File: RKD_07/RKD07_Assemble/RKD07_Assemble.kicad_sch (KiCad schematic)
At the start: 147 parts, among them J1 Conn_01x02_Socket, J2 Conn_01x24, J3 Conn_01x24, J4 Conn_01x24, SW1 SW_Push, SW10 SW_Push, SW11 SW_Push, SW12 SW_Push, SW13 SW_Push, SW14 SW_Push, SW15 SW_Push, SW16 SW_Push, SW17 SW_Push, SW18 SW_Push, SW19 SW_Push, SW2 SW_Push, SW20 SW_Push, SW21 SW_Push, SW22 SW_Push, SW23 SW_Push, SW24 SW_Push, SW25 SW_Push, SW26 SW_Push, SW27 SW_Push, SW28 SW_Push, SW29 SW_Push, SW3 SW_Push, SW30 RotaryEncoder_Switch, SW31 SW_Push, SW4 SW_Push, SW5 SW_Push, SW51 SW_Push, SW52 SW_Push, SW53 SW_Push, SW54 SW_Push, SW55 SW_Push, SW56 SW_Push, SW57 SW_Push, SW58 SW_Push, SW59 SW_Push, SW6 SW_Push, SW60 SW_Push, SW61 SW_Push, SW62 SW_Push, SW63 SW_Push, SW64 SW_Push, SW65 SW_Push, SW66 SW_Push, SW67 SW_Push, SW68 SW_Push, SW69 SW_Push, SW7 SW_Push, SW70 SW_Push, SW71 SW_Push, SW72 SW_Push, SW73 SW_Push, SW74 SW_Push, SW75 SW_Push, SW76 SW_Push, SW77 SW_Push, SW78 SW_Push, SW79 SW_Push, SW8 SW_Push, SW80 SW_Push, SW81 SW_Push, SW82 SW_Push, SW83 SW_Push, SW84 SW_Push, SW85 SW_Push, SW86 SW_Push, SW87 SW_Push, SW88 SW_Push, SW89 SW_Push, SW9 SW_Push, SW90 SW_Push, U1 Pico

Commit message: RKD07 一時保存
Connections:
- net GP18_R is gone; now on net SDA/SCK_R: J3.14 (Pin_14), J4.11 (Pin_11)
- net GP19_R is gone; now on net SCL/TX_R: J3.13 (Pin_13), J4.12 (Pin_12)
- net GND_L: now also U1.23 (GND)
- net SCL/TX_L: now also J2.12 (Pin_12), U1.25 (GPIO19); no longer J2.1 (Pin_1), U1.20 (GPIO15)
- net SCL/TX_R: no longer J3.24 (Pin_24), J4.1 (Pin_1)
- net SDA/SCK_L: now also J2.11 (Pin_11), U1.24 (GPIO18); no longer J2.2 (Pin_2), U1.19 (GPIO14)
- net SDA/SCK_R: no longer J3.23 (Pin_23), J4.2 (Pin_2)
- new net GP14_R: J3.23 (Pin_23), J4.2 (Pin_2)
- new net GP15_R: J3.24 (Pin_24), J4.1 (Pin_1)
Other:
- note added: "GND VCC 3V3 GP28 GP27 GP26 GP25 GP24 GP23 GP22 GP21 GP20 GP19 GP18 GP17 GP16 GP08 GP09 GP10 GP11 GP12 GP13 GP14 GP15"
- moved on the sheet: J2

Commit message: RD07配線
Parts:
- added J10, J9: Conn_01x04, Connector_PinSocket_2.54mm:PinSocket_1x04_P2.54mm_Horizontal, symbol Connector_Generic:Conn_01x04
- added J5, J6: Qwiic_RA, SparkFun-Connector:JST_SMD_1.0mm-4_Black, symbol SparkFun-Connector:Qwiic_Right_Angle
- added J7, J8: Conn_01x06, Connector_FFC-FPC:Hirose_FH12-6S-0.5SH_1x06-1MP_P0.50mm_Horizontal, symbol Connector_Generic:Conn_01x06
- added R1, R2: R, Resistor_THT:R_Axial_DIN0207_L6.3mm_D2.5mm_P10.16mm_Horizontal, symbol Device:R
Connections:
- net GP12_R is gone; now on net ROW1_R: J3.21 (Pin_21), J4.4 (Pin_4)
- net GP13_R is gone; now on net ROW2_R: J3.22 (Pin_22), J4.3 (Pin_3)
- net GP14_R is gone; now on net ROW3_R: J3.23 (Pin_23), J4.2 (Pin_2)
- net GP15_R is gone; now on net ROW4_R: J3.24 (Pin_24), J4.1 (Pin_1)
- net GP20_R is gone; now on net COL6_R: J3.12 (Pin_12), J4.13 (Pin_13)
- net GP21_R is gone; now on net COL7_R: J3.11 (Pin_11), J4.14 (Pin_14)
- net GP22_R is gone; now on net COL8_R: J3.10 (Pin_10), J4.15 (Pin_15)
- net GP23_R is gone; now on net COL9_R: J3.9 (Pin_9), J4.16 (Pin_16)
- net GP24_R is gone; now on net COL10_R: J3.8 (Pin_8), J4.17 (Pin_17)
- net GP25_R is gone; now on net COL11_R: J3.7 (Pin_7), J4.18 (Pin_18)
- net GP26_R is gone; now on net COL12_R: J3.6 (Pin_6), J4.19 (Pin_19)
- net GP27_R is gone; now on net COL13_R: J3.5 (Pin_5), J4.20 (Pin_20)
- net GP28_R is gone; now on net ROW0_R: J3.4 (Pin_4), J4.21 (Pin_21)
- net 3v3_L: now also J5.2 (Pin_2), J8.6 (Pin_6)
- net 3v3_R: now also J6.2 (Pin_2), J7.6 (Pin_6), J9.2 (Pin_2), J9.3 (Pin_3), R1.1, R2.1
- net COL0_L: now also J2.10 (Pin_10), U1.2 (GPIO1)
- net COL1_L: now also J2.9 (Pin_9), U1.4 (GPIO2)
- net COL2_L: now also J2.8 (Pin_8), U1.5 (GPIO3)
- net COL3_L: now also J2.7 (Pin_7), U1.6 (GPIO4)
- net COL4_L: now also J2.6 (Pin_6), U1.7 (GPIO5)
- net COL5_L: now also J2.5 (Pin_5), U1.9 (GPIO6)
- net GND_L: now also U1.28 (GND), J5.1 (Pin_1), J8.1 (Pin_1), J8.5 (Pin_5)
- net GND_R: now also J6.1 (Pin_1), J7.1 (Pin_1), J7.5 (Pin_5)
- net RE_A: now also U1.15 (GPIO11), J10.1 (Pin_1)
- net RE_B: now also U1.16 (GPIO12), J10.4 (Pin_4)
- net ROW0_L: now also J2.21 (Pin_21), U1.1 (GPIO0)
- net ROW1_L: now also J2.4 (Pin_4), U1.10 (GPIO7)
- net ROW2_L: now also J2.3 (Pin_3), U1.11 (GPIO8)
- net ROW3_L: now also J2.2 (Pin_2), U1.12 (GPIO9)
- net ROW4_L: now also J2.1 (Pin_1), U1.14 (GPIO10)
- net SCL/TX_L: now also J10.3 (Pin_3), J5.4 (Pin_4)
- net SCL/TX_R: now also J6.4 (Pin_4), J7.3 (Pin_3), J9.1 (Pin_1), R1.2
- net SDA/SCK_L: now also J10.2 (Pin_2), J5.3 (Pin_3)
- net SDA/SCK_R: now also J6.3 (Pin_3), J7.2 (Pin_2), J9.4 (Pin_4), R2.2
- net SCK_L: now reaches U1.19 (GPIO14)
- net SCK_L: now also J8.2 (Pin_2)
- net TX_L: now reaches U1.20 (GPIO15)
- net TX_L: now also J8.3 (Pin_3)
- net COL6_L: now reaches U1.21 (GPIO16)
- net COL6_L: now also J2.13 (Pin_13)
- net COL7_L: now reaches U1.22 (GPIO17)
- net COL7_L: now also J2.14 (Pin_14)
- net COL8_L: now reaches U1.26 (GPIO20)
- net COL8_L: now also J2.15 (Pin_15)
- net COL9_L: now reaches U1.27 (GPIO21)
- net COL9_L: now also J2.16 (Pin_16)
- net COL10_L: now reaches U1.29 (GPIO22)
- net COL10_L: now also J2.17 (Pin_17)
- net COL11_L: now reaches U1.31 (GPIO26_ADC0)
- net COL11_L: now also J2.18 (Pin_18)
- net COL12_L: now reaches U1.32 (GPIO27_ADC1)
- net COL12_L: now also J2.19 (Pin_19)
- net COL13_L: now reaches U1.34 (GPIO28_ADC2)
- net COL13_L: now also J2.20 (Pin_20)
- net GP08_R renamed COL2_R
- net GP09_R renamed COL3_R
- net GP10_R renamed COL4_R
- net GP11_R renamed COL5_R
- net GP16_R renamed COL1_R
- net GP17_R renamed COL0_R
- no-connect marks 8 -> 15
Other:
- note added: "CS"
- note added: "MOTION"
- note added: "Resist for i2c"

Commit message: 07 Modify
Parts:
- J10: footprint Connector_PinSocket_2.54mm:PinSocket_1x04_P2.54mm_Horizontal -> Connector_PinHeader_2.54mm:PinHeader_1x04_P2.54mm_Horizontal
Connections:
- net RE_A: now also J10.4 (Pin_4); no longer J10.1 (Pin_1)
- net RE_B: now also J10.1 (Pin_1); no longer J10.4 (Pin_4)
- net SCL/TX_L: now also J10.2 (Pin_2); no longer J10.3 (Pin_3)
- net SDA/SCK_L: now also J10.3 (Pin_3); no longer J10.2 (Pin_2)
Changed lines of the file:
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@@
 		)
 	)
-	(global_label "COL7_L"
+	(global_label "SCL{slash}TX_L"
 		(shape input)
-		(at 90.17 100.33 0)
+		(at 88.9 386.08 180)
 		(fields_autoplaced yes)
 		(effects
@@
 				(size 1.27 1.27)
 			)
-			(justify left)
+			(justify right)
 		)
 		(property "Intersheetrefs" "${INTERSHEET_REFS}"
-			(at 99.989 100.33 0)
+			(at 76.9039 386.08 0)
 			(effects
 				(font
 					(size 1.27 1.27)
 				)
-				(justify left)
+				(justify right)
 				(hide yes)
 			)
 		)
 	)
-	(global_label "SDA{slash}SCK_L"
+	(global_label "COL7_L"
 		(shape input)
-		(at 88.9 386.08 180)
+		(at 90.17 100.33 0)
 		(fields_autoplaced yes)
 		(effects
@@
 				(size 1.27 1.27)
 			)
-			(justify right)
+			(justify left)
 		)
 		(property "Intersheetrefs" "${INTERSHEET_REFS}"
-			(at 75.271 386.08 0)
+			(at 99.989 100.33 0)
 			(effects
 				(font
 					(size 1.27 1.27)
 				)
-				(justify right)
+				(justify left)
 				(hide yes)
 			)
@@
 		)
 	)
-	(global_label "RE_B"
-		(shape input)
-		(at 88.9 391.16 180)
-		(fields_autoplaced yes)
-		(effects
-			(font
-				(size 1.27 1.27)
-			)
-			(justify right)
-		)
-		(property "Intersheetrefs" "${INTERSHEET_REFS}"
-			(at 81.2582 391.16 0)
-			(effects
-				(font
-					(size 1.27 1.27)
-				)
-				(justify right)
-				(hide yes)
-			)
-		)
-	)
 	(global_label "COL9_R"
 		(shape input)
@@
 		)
 	)
+	(global_label "SDA{slash}SCK_L"
+		(shape input)
+		(at 88.9 388.62 180)
+		(fields_autoplaced yes)
+		(effects
+			(font
+				(size 1.27 1.27)
+			)
+			(justify right)
+		)
+		(property "Intersheetrefs" "${INTERSHEET_REFS}"
+			(at 75.271 388.62 0)
+			(effects
+				(font
+					(size 1.27 1.27)
+				)
+				(justify right)
+				(hide yes)
+			)
+		)
+	)
 	(global_label "ROW4_L"
 		(shape input)
@@
 		)
 	)
-	(global_label "RE_A"
-		(shape input)
-		(at 88.9 383.54 180)
-		(fields_autoplaced yes)
-		(effects
-			(font
-				(size 1.27 1.27)
-			)
-			(justify right)
-		)
-		(property "Intersheetrefs" "${INTERSHEET_REFS}"
-			(at 81.4396 383.54 0)
-			(effects
-				(font
-					(size 1.27 1.27)
-				)
-				(justify right)
-				(hide yes)
-			)
-		)
-	)
 	(global_label "SCL{slash}TX_L"
 		(shape input)
@@
 		)
 	)
-	(global_label "SCL{slash}TX_L"
+	(global_label "RE_A"
 		(shape input)
-		(at 259.08 157.48 0)
+		(at 88.9 391.16 180)
 		(fields_autoplaced yes)
 		(effects
@@
 				(size 1.27 1.27)
 			)
-			(justify left)
+			(justify right)
 		)
 		(property "Intersheetrefs" "${INTERSHEET_REFS}"
-			(at 271.0761 157.48 0)
+			(at 81.4396 391.16 0)
 			(effects
 				(font
 					(size 1.27 1.27)
 				)
-				(justify left)
+				(justify right)
 				(hide yes)
 			)
 		)
 	)
-	(global_label "COL0_L"
+	(global_label "SCL{slash}TX_L"
 		(shape input)
-		(at 259.08 162.56 0)
+		(at 259.08 157.48 0)
 		(fields_autoplaced yes)
 		(effects
@@
 		)
 		(property "Intersheetrefs" "${INTERSHEET_REFS}"
-			(at 268.899 162.56 0)
+			(at 271.0761 157.48 0)
 			(effects
 				(font
@@
 		)
 	)
-	(global_label "COL12_R"
+	(global_label "COL0_L"
 		(shape input)
-		(at 292.1 139.7 180)
+		(at 259.08 162.56 0)
 		(fields_autoplaced yes)
 		(effects
@@
 				(size 1.27 1.27)
 			)
-			(justify right)
+			(justify left)
 		)
 		(property "Intersheetrefs" "${INTERSHEET_REFS}"
-			(at 280.8296 139.7 0)
+			(at 268.899 162.56 0)
 			(effects
 				(font
 					(size 1.27 1.27)
 				)
-				(justify right)
+				(justify left)
 				(hide yes)
 			)
 		)
 	)
-	(global_label "RE_B"
+	(global_label "COL12_R"
 		(shape input)
-		(at 134.62 381 180)
+		(at 292.1 139.7 180)
 		(fields_autoplaced yes)
 		(effects
@@
 		)
 		(property "Intersheetrefs" "${INTERSHEET_REFS}"
-			(at 126.9782 381 0)
+			(at 280.8296 139.7 0)
 			(effects
 				(font
@@
 		)
 	)
-	(global_label "SCL{slash}TX_L"
+	(global_label "RE_B"
 		(shape input)
-		(at 88.9 388.62 180)
+		(at 134.62 381 180)
 		(fields_autoplaced yes)
 		(effects
@@
 		)
 		(property "Intersheetrefs" "${INTERSHEET_REFS}"
-			(at 76.9039 388.62 0)
+			(at 126.9782 381 0)
 			(effects
 				(font
@@
 		)
 	)
+	(global_label "RE_B"
+		(shape input)
+		(at 88.9 383.54 180)
+		(fields_autoplaced yes)
+		(effects
+			(font
+				(size 1.27 1.27)
+			)
+			(justify right)
+		)
+		(property "Intersheetrefs" "${INTERSHEET_REFS}"
+			(at 81.2582 383.54 0)
+			(effects
+				(font
+					(size 1.27 1.27)
+				)
+				(justify right)
+				(hide yes)
+			)
+		)
+	)
 	(global_label "COL9_L"
 		(shape input)
@@
 			)
 		)
-		(property "Footprint" "Connector_PinSocket_2.54mm:PinSocket_1x04_P2.54mm_Horizontal"
+		(property "Footprint" "Connector_PinHeader_2.54mm:PinHeader_1x04_P2.54mm_Horizontal"
 			(at 93.98 386.08 0)
 			(effects

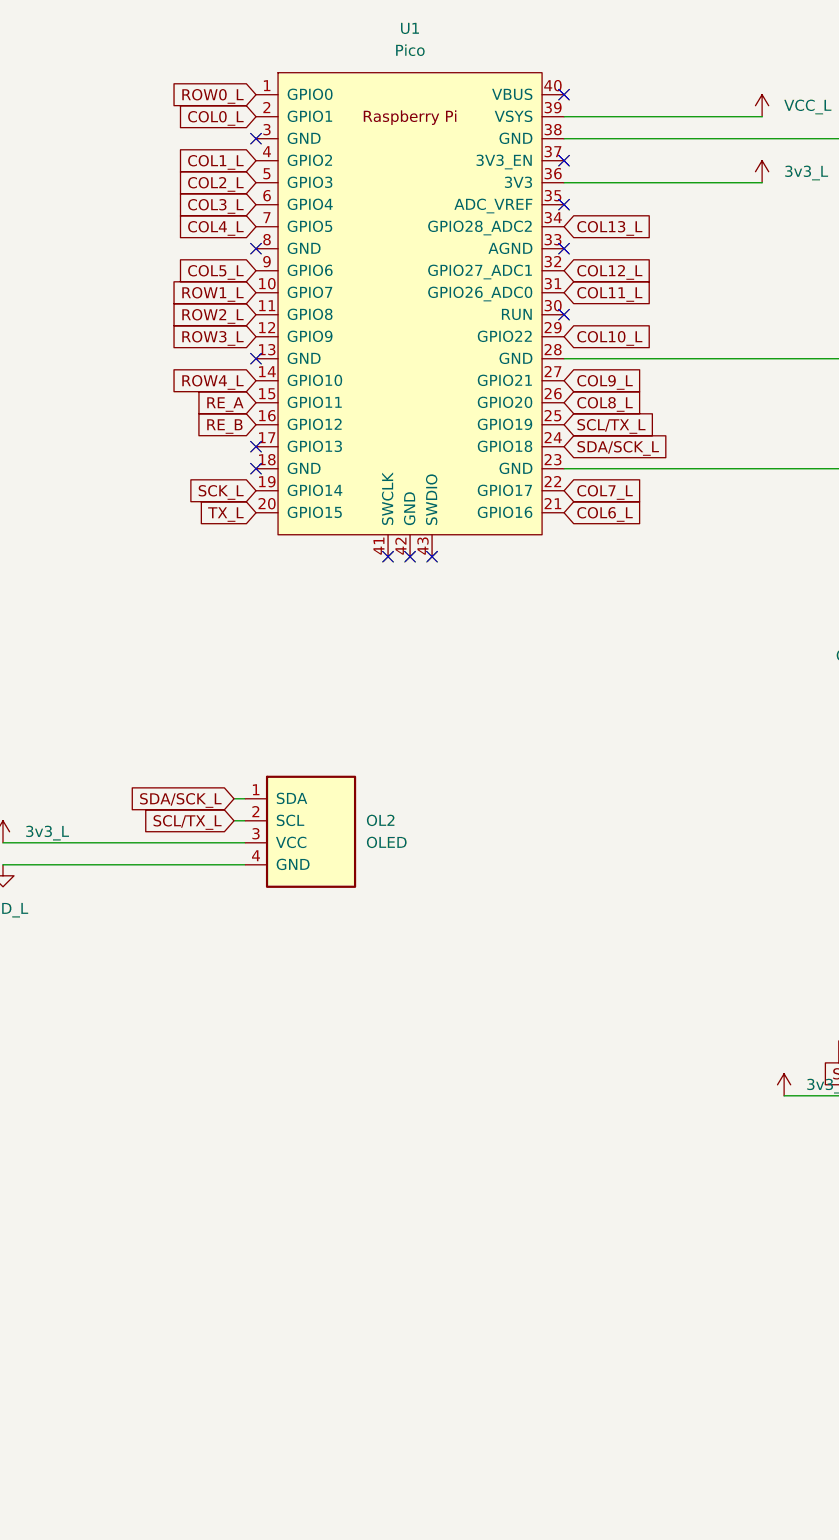
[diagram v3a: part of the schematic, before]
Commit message: TRRS追加
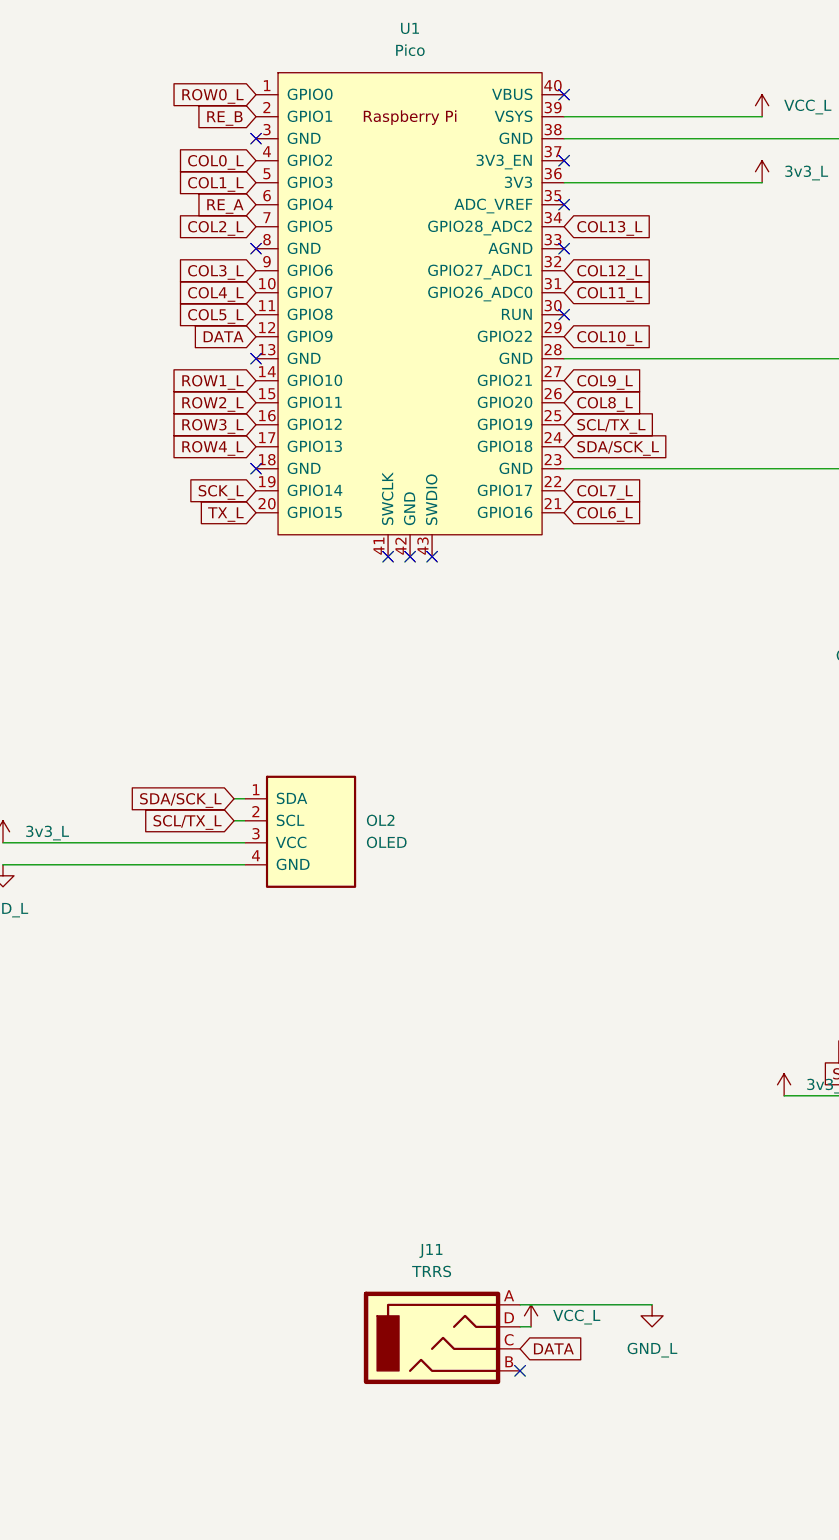
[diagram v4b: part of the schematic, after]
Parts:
- added J11: TRRS, BrownSugar_KBD:TRRS_PJ-320A, symbol BrownSugar_KBD:TRRS
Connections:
- net COL0_L: now also U1.4 (GPIO2); no longer U1.2 (GPIO1)
- net COL1_L: now also U1.5 (GPIO3); no longer U1.4 (GPIO2)
- net COL2_L: now also U1.7 (GPIO5); no longer U1.5 (GPIO3)
- net COL3_L: now also U1.9 (GPIO6); no longer U1.6 (GPIO4)
- net COL4_L: now also U1.10 (GPIO7); no longer U1.7 (GPIO5)
- net COL5_L: now also U1.11 (GPIO8); no longer U1.9 (GPIO6)
- net GND_L: now also J11.A
- net RE_A: now also U1.6 (GPIO4); no longer U1.15 (GPIO11)
- net RE_B: now also U1.2 (GPIO1); no longer U1.16 (GPIO12)
- net ROW1_L: now also U1.14 (GPIO10); no longer U1.10 (GPIO7)
- net ROW2_L: now also U1.15 (GPIO11); no longer U1.11 (GPIO8)
- net ROW3_L: now also U1.16 (GPIO12); no longer U1.12 (GPIO9)
- net ROW4_L: now also U1.17 (GPIO13); no longer U1.14 (GPIO10)
- net VCC_L: now also J11.D
- new net DATA: J11.C, U1.12 (GPIO9)

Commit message: 07Geek追加
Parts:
- added J12: Conn_01x06, Connector_FFC-FPC:Hirose_FH12-6S-0.5SH_1x06-1MP_P0.50mm_Horizontal, symbol Connector_Generic:Conn_01x06
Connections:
- net 3v3_R: now also J12.4 (Pin_4)
- net GND_R: now also J12.3 (Pin_3)
- net SCL/TX_R: now also J12.5 (Pin_5)
- net SDA/SCK_R: now also J12.6 (Pin_6)
- no-connect marks 15 -> 17

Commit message: 穴一など修正
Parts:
- added J13: Conn_01x06, Connector_FFC-FPC:Hirose_FH12-6S-0.5SH_1x06-1MP_P0.50mm_Horizontal, symbol Connector_Generic:Conn_01x06
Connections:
- net 3v3_L: now also J13.3 (Pin_3)
- net 3v3_R: now also J12.3 (Pin_3); no longer J12.4 (Pin_4)
- net GND_L: now also J13.4 (Pin_4); no longer U1.23 (GND)
- net GND_R: now also J12.4 (Pin_4); no longer J12.3 (Pin_3)
- net SCL/TX_L: now also J13.2 (Pin_2)
- net SCL/TX_R: now also J12.2 (Pin_2), J9.4 (Pin_4); no longer J12.5 (Pin_5), J9.1 (Pin_1)
- net SDA/SCK_L: now also J13.1 (Pin_1)
- net SDA/SCK_R: now also J12.1 (Pin_1), J9.1 (Pin_1); no longer J12.6 (Pin_6), J9.4 (Pin_4)
- no-connect marks 17 -> 20
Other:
- note added: "GeekRabit_Trackpad"
- note added: "Nogikesuy_TrackBall"
- note added: "Nogikesuya_TrackBall"
- moved on the sheet: J12

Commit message: 07 I2C抵抗追加
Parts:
- added R3, R4: R, Resistor_THT:R_Axial_DIN0207_L6.3mm_D2.5mm_P10.16mm_Horizontal, symbol Device:R
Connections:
- net 3v3_L: now also R3.1, R4.1
- net SCL/TX_L: now also R3.2
- net SDA/SCK_L: now also R4.2

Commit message: QWICC位置など調整
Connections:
- net COL0_L: now also U1.5 (GPIO3); no longer U1.4 (GPIO2)
- net COL1_L: now also U1.6 (GPIO4); no longer U1.5 (GPIO3)
- net COL2_L: now also U1.9 (GPIO6); no longer U1.7 (GPIO5)
- net COL3_L: now also U1.10 (GPIO7); no longer U1.9 (GPIO6)
- net COL4_L: now also U1.11 (GPIO8); no longer U1.10 (GPIO7)
- net COL5_L: now also U1.12 (GPIO9); no longer U1.11 (GPIO8)
- net DATA: now also U1.1 (GPIO0); no longer U1.12 (GPIO9)
- net RE_A: now also U1.7 (GPIO5); no longer U1.6 (GPIO4)
- net RE_B: now also U1.4 (GPIO2); no longer U1.2 (GPIO1)
- net ROW0_L: now also U1.2 (GPIO1); no longer U1.1 (GPIO0)
